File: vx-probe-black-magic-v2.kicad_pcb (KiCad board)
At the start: 2 copper layers, 72.4 x 41.9 mm, 41 parts, among them P1 USB MINI B, P10 CONN_01X01, P11 CONN_01X11, P2 +5v power input, P3 +5v external input, P4 CONN_02X05, P5 CONN_01X04, P6 swdio/jtag, P7 CONN_01X01, P8 CONN_01X01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

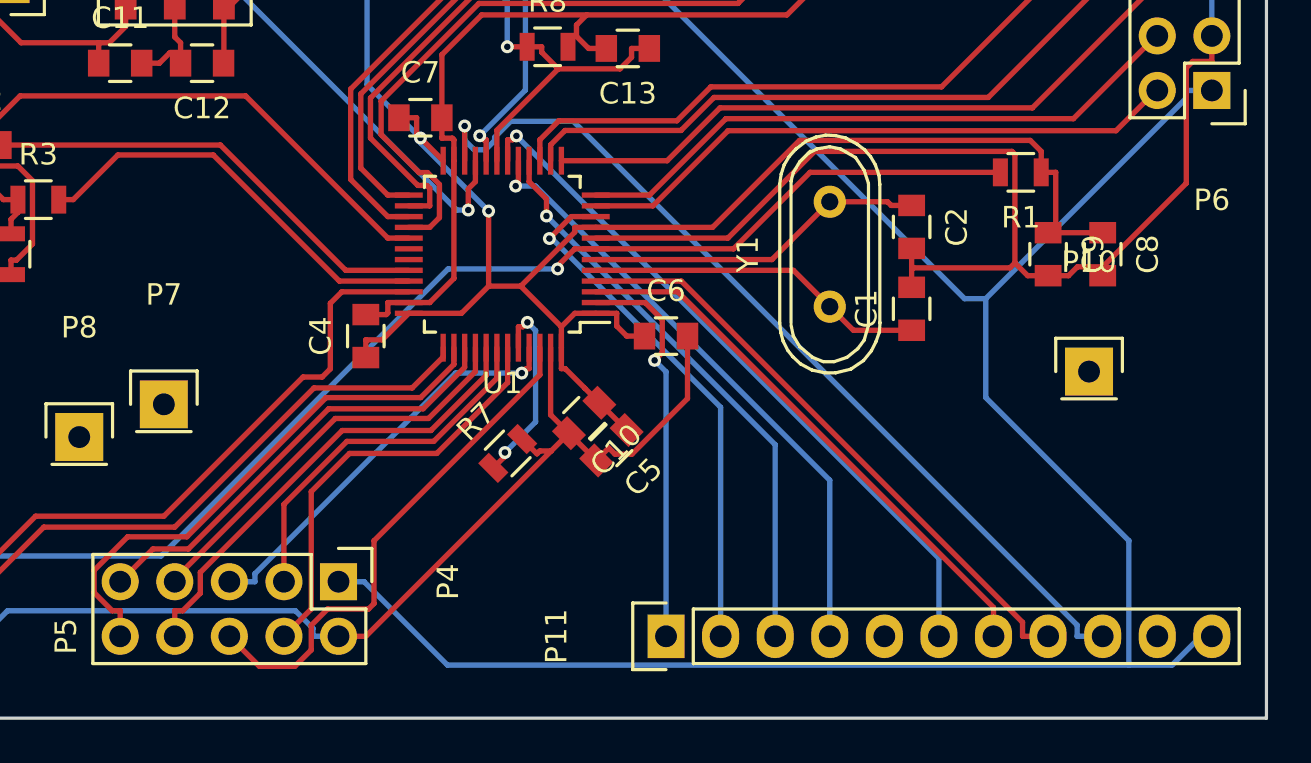
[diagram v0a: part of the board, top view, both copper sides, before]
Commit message: reorganized the unused pins connector
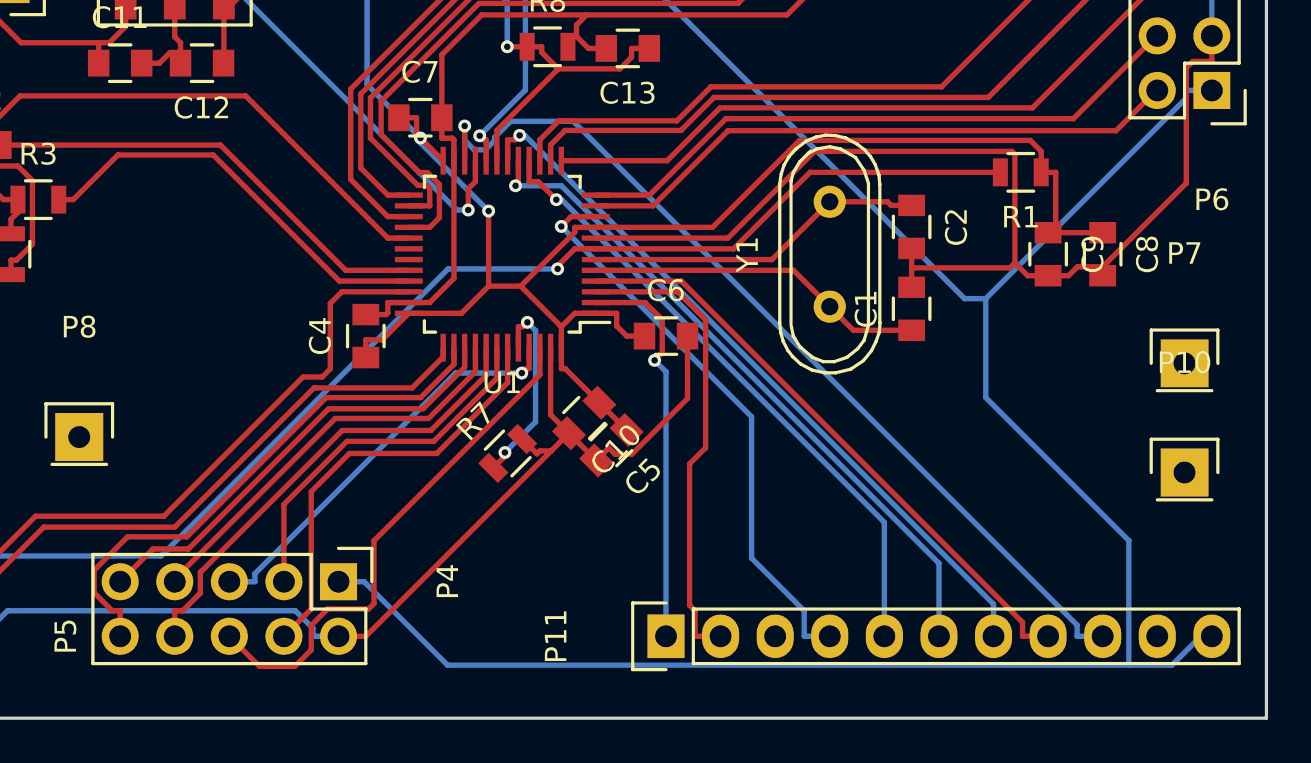
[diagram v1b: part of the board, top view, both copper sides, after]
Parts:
- moved P7 47.5 mm to (115.6, 64.8)
- moved P10 6.47 mm to (115.6, 69.8)
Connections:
- P11 pad 2: /x4 -> /x2
- P11 pad 3: /x5 -> Net-(P11-Pad3)
- P11 pad 4: /x6 -> /x4
- P11 pad 5: Net-(P11-Pad5) -> /x5
- P11 pad 6: /x7 -> /x6
- P11 pad 7: /x2 -> /x7
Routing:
- net /x2: track 25.9 -> 22.0 mm
- net /x6: track 28.8 -> 31.6 mm
- net /x5: track 26.9 -> 29.4 mm
- net /x4: track 24.5 -> 26.7 mm
- net /x7: track 32.9 -> 34.2 mm

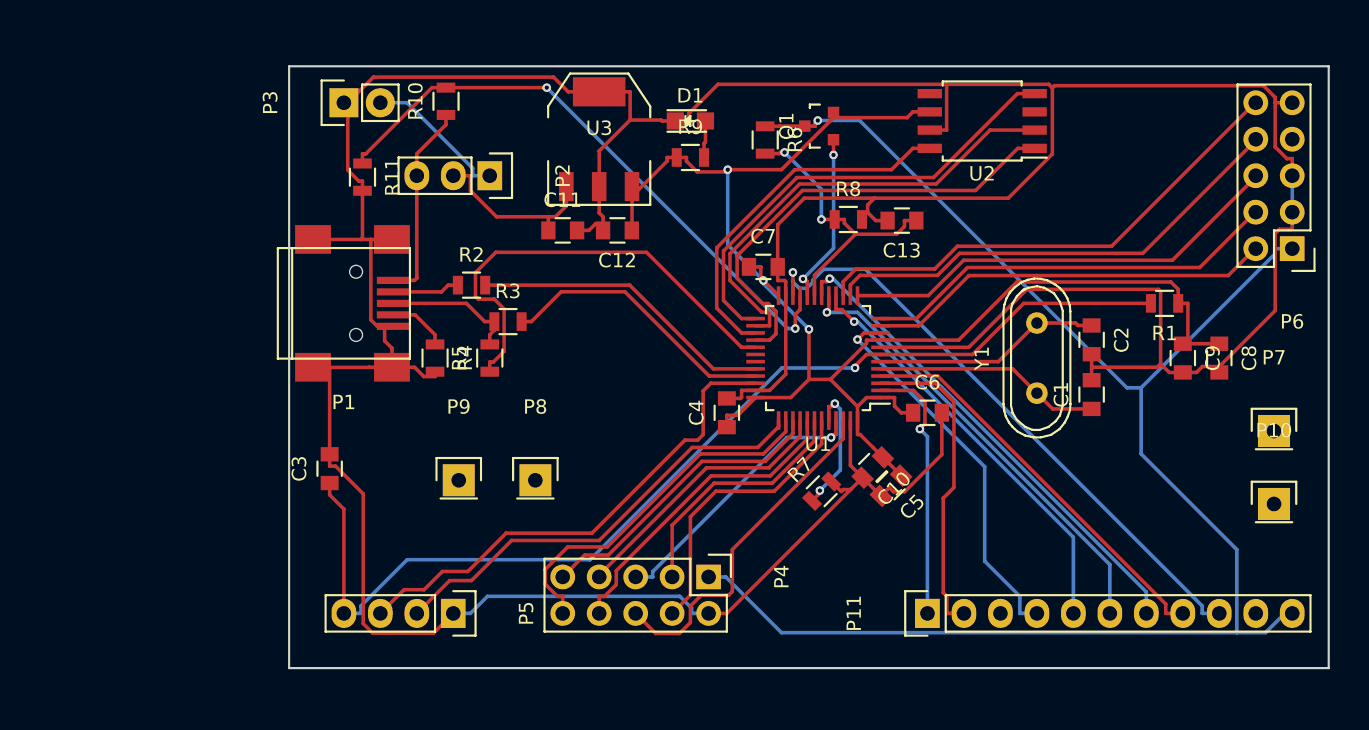
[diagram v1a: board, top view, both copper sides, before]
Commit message: placed and routed the reset button and a serial port
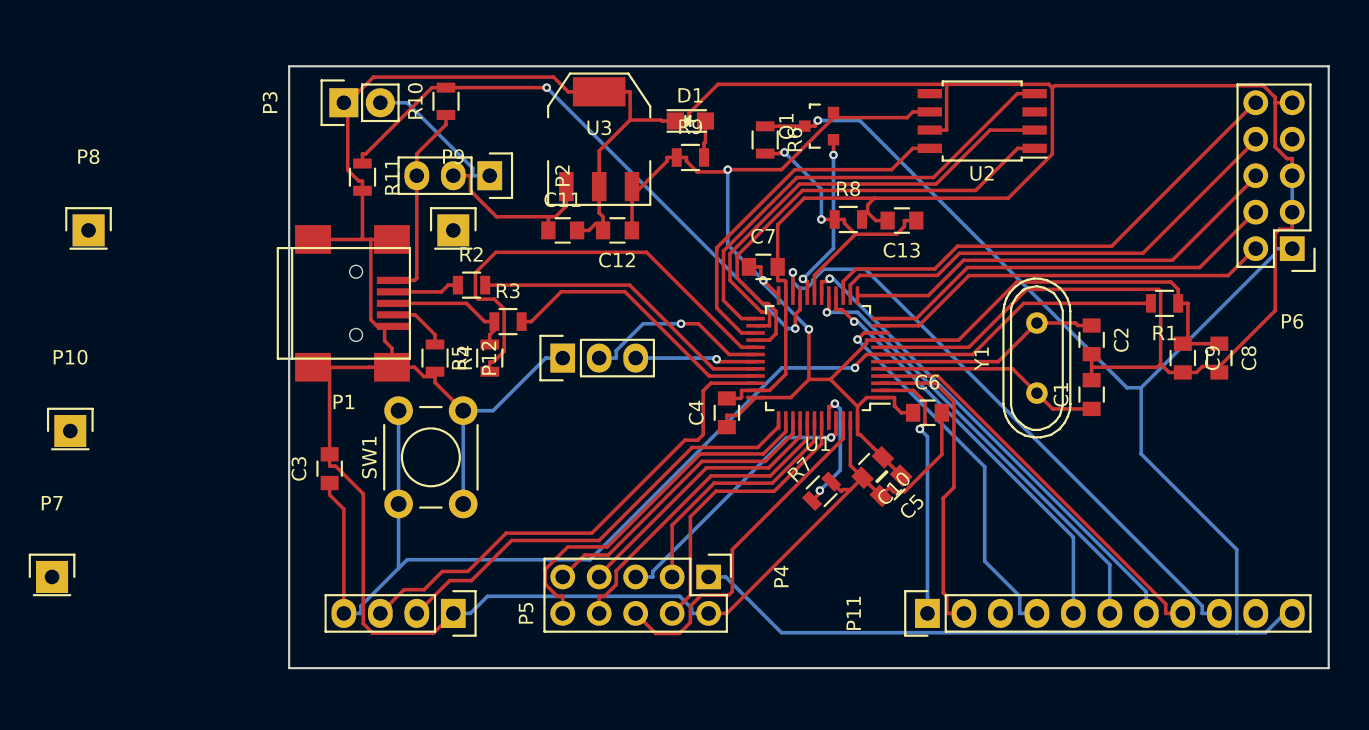
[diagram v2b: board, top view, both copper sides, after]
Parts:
- added P12: CONN_01X03, Pin_Headers:Pin_Header_Straight_1x03, F.Cu at (66.0, 59.7)
- added SW1: SW_PUSH, Buttons_Switches_ThroughHole:SW_PUSH_6mm, F.Cu at (54.6, 69.8)
- moved P7 85.7 mm to (30.5, 74.9)
- moved P10 84.0 mm to (31.8, 64.8)
- moved P8 35.6 mm to (33.0, 50.8)
- moved P9 17.4 mm to (58.4, 50.8)
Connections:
- U1 pad 30: Net-(U1-Pad30) -> /U1_TX
- U1 pad 31: Net-(U1-Pad31) -> /U1_RX
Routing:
- net GND: track 303.7 -> 322.0 mm
- net /U1_TX: track 0.00 -> 13.1 mm, vias 0 -> 1
- net /PROG_NRST: track 75.0 -> 86.0 mm
- net /U1_RX: track 0.00 -> 8.45 mm, vias 0 -> 1

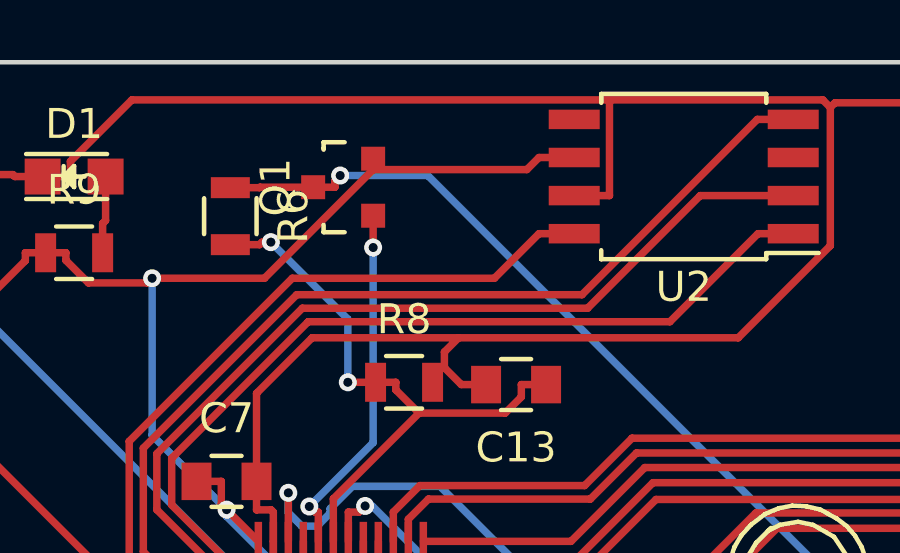
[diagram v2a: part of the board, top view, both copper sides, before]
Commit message: added a pull-up resistor on the target power enable switch (pmosfet)
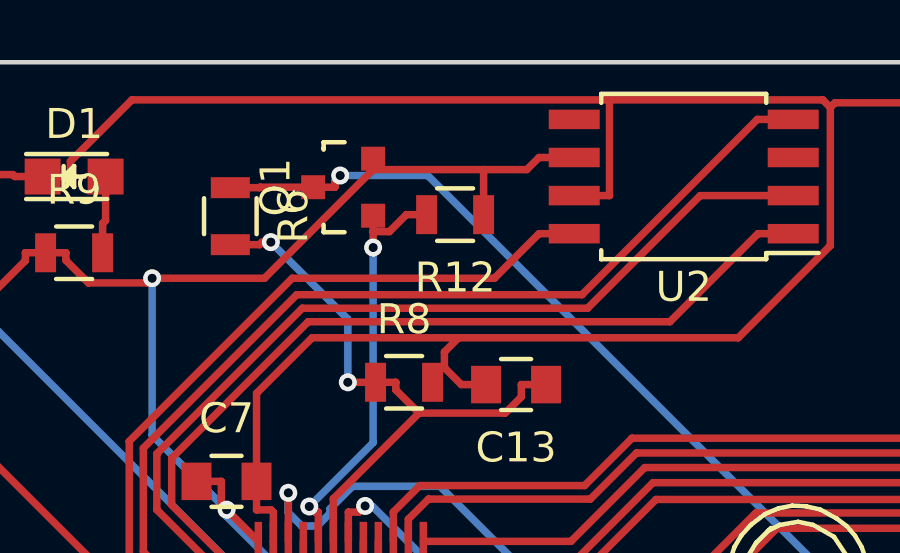
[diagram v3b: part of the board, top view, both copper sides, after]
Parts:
- added R12: 10k, Resistors_SMD:R_0805, F.Cu at (87.6, 44.5)
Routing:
- net /TPWR_CTRL: track 11.9 -> 13.9 mm
- net +3V3: track 105.2 -> 106.7 mm
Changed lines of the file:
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@@
 (kicad_pcb (version 4) (host pcbnew 4.0.4-stable)
   (general
-    (links 117)
-    (no_connects 1)
+    (links 119)
+    (no_connects 0)
     (area 46.914999 39.294999 119.455001 81.355001)
     (thickness 1.6)
     (drawings 11)
-    (tracks 573)
+    (tracks 580)
     (zones 0)
-    (modules 43)
+    (modules 44)
     (nets 59)
   )
@@
       (scale (xyz 1 1 1))
       (rotate (xyz 0 0 90))
+    )
+  )
+  (module Resistors_SMD:R_0805 (layer F.Cu)
+    (at 87.63 44.45 180)
+    (descr "Resistor SMD 0805, reflow soldering, Vishay (see dcrcw.pdf)")
+    (tags "resistor 0805")
+    (attr smd)
+    (fp_text reference R12 (at 0 -2.1 180) (layer F.SilkS)
+      (effects (font (size 1 1) (thickness 0.15)))
+    )
+    (fp_text value 10k (at 0 2.1 180) (layer F.Fab)
+      (effects (font (size 1 1) (thickness 0.15)))
+    )
+    (fp_line (start -1.6 -1) (end 1.6 -1) (layer F.CrtYd) (width 0.05))
+    (fp_line (start -1.6 1) (end 1.6 1) (layer F.CrtYd) (width 0.05))
+    (fp_line (start -1.6 -1) (end -1.6 1) (layer F.CrtYd) (width 0.05))
+    (fp_line (start 1.6 -1) (end 1.6 1) (layer F.CrtYd) (width 0.05))
+    (fp_line (start 0.6 0.875) (end -0.6 0.875) (layer F.SilkS) (width 0.15))
+    (fp_line (start -0.6 -0.875) (end 0.6 -0.875) (layer F.SilkS) (width 0.15))
+    (pad 1 smd rect (at -0.95 0 180) (size 0.7 1.3) (layers F.Cu F.Paste F.Mask)
+      (net 4 +3V3))
+    (pad 2 smd rect (at 0.95 0 180) (size 0.7 1.3) (layers F.Cu F.Paste F.Mask)
+      (net 38 /TPWR_CTRL))
+    (model Resistors_SMD.3dshapes/R_0805.wrl
+      (at (xyz 0 0 0))
+      (scale (xyz 1 1 1))
+      (rotate (xyz 0 0 0))
     )
   )
@@
   (segment (start 108.9 55.88) (end 108.9 54.9047) (width 0.25) (layer F.Cu) (net 4))
   (segment (start 84.897 42.5856) (end 84.897 42.9482) (width 0.25) (layer F.Cu) (net 4))
-  (segment (start 90.0215 42.9482) (end 84.897 42.9482) (width 0.25) (layer F.Cu) (net 4))
+  (segment (start 81.2754 46.5698) (end 84.897 42.9482) (width 0.25) (layer F.Cu) (net 4))
+  (segment (start 77.5298 46.5698) (end 81.2754 46.5698) (width 0.25) (layer F.Cu) (net 4))
+  (segment (start 90.0215 42.9482) (end 88.5758 42.9482) (width 0.25) (layer F.Cu) (net 4))
   (segment (start 90.4247 42.545) (end 90.0215 42.9482) (width 0.25) (layer F.Cu) (net 4))
   (segment (start 91.6 42.545) (end 90.4247 42.545) (width 0.25) (layer F.Cu) (net 4))
-  (segment (start 81.2754 46.5698) (end 84.897 42.9482) (width 0.25) (layer F.Cu) (net 4))
-  (segment (start 77.5298 46.5698) (end 81.2754 46.5698) (width 0.25) (layer F.Cu) (net 4))
+  (segment (start 88.5758 42.9482) (end 84.897 42.9482) (width 0.25) (layer F.Cu) (net 4))
+  (segment (start 88.58 42.9524) (end 88.58 44.45) (width 0.25) (layer F.Cu) (net 4))
+  (segment (start 88.5758 42.9482) (end 88.58 42.9524) (width 0.25) (layer F.Cu) (net 4))
   (segment (start 109.22 58.69) (end 109.575 58.69) (width 0.25) (layer F.Cu) (net 4))
   (segment (start 109.575 58.69) (end 111.76 58.69) (width 0.25) (layer F.Cu) (net 4))
@@
   (segment (start 84.897 52.0507) (end 84.897 45.5458) (width 0.25) (layer B.Cu) (net 38))
   (segment (start 82.7694 54.1783) (end 84.897 52.0507) (width 0.25) (layer B.Cu) (net 38))
-  (segment (start 84.897 45.5458) (end 84.897 44.4856) (width 0.25) (layer F.Cu) (net 38))
+  (segment (start 85.439 45.0157) (end 84.897 45.0157) (width 0.25) (layer F.Cu) (net 38))
+  (segment (start 86.0047 44.45) (end 85.439 45.0157) (width 0.25) (layer F.Cu) (net 38))
+  (segment (start 86.68 44.45) (end 86.0047 44.45) (width 0.25) (layer F.Cu) (net 38))
+  (segment (start 84.897 45.5458) (end 84.897 45.0157) (width 0.25) (layer F.Cu) (net 38))
+  (segment (start 84.897 45.0157) (end 84.897 44.4856) (width 0.25) (layer F.Cu) (net 38))
   (segment (start 78.4947 58.94) (end 79.47 58.94) (width 0.25) (layer F.Cu) (net 39))
   (segment (start 71.8787 52.324) (end 78.4947 58.94) (width 0.25) (layer F.Cu) (net 39))

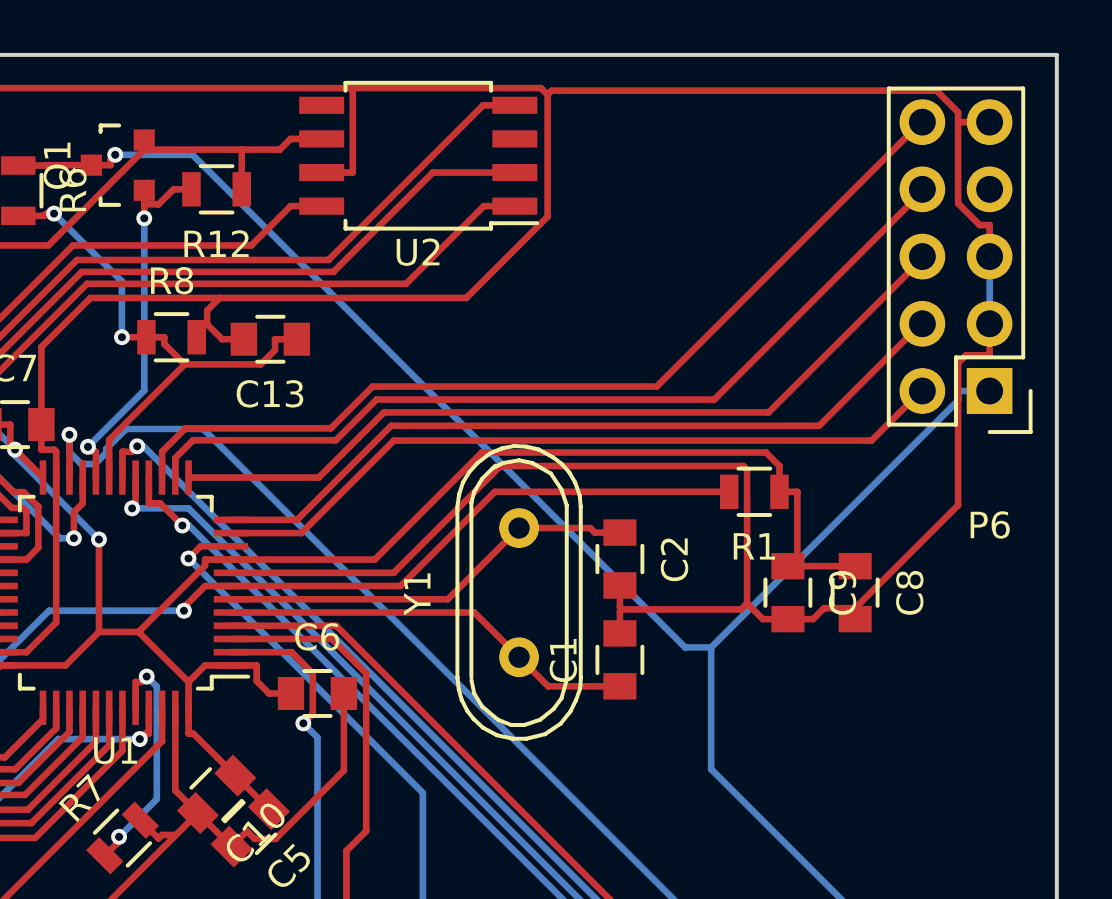
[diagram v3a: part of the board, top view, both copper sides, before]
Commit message: moved the crystal closer to the microcontroller
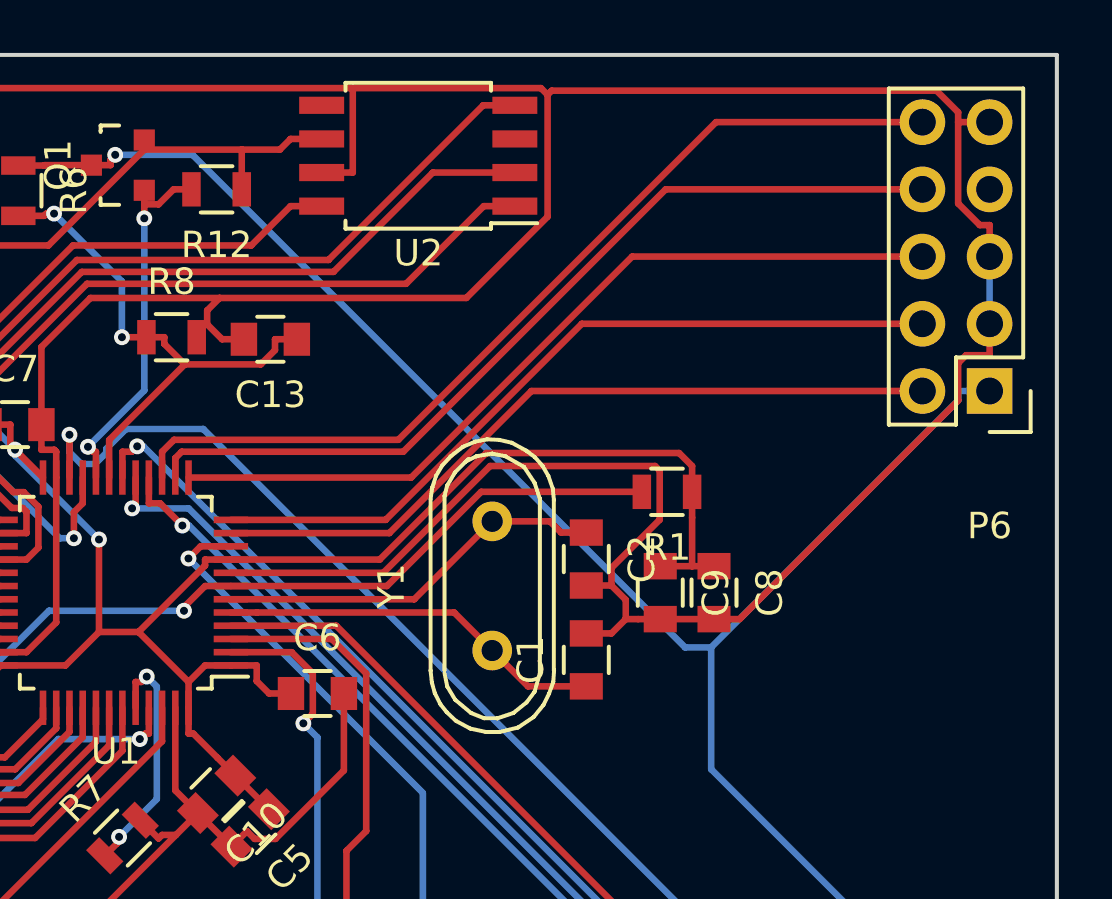
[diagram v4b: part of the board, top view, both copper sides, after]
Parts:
- moved C8 5.33 mm to (106.4, 59.7)
- moved C9 4.83 mm to (104.4, 59.7)
- moved R1 3.30 mm to (104.6, 55.9)
- moved C1 1.27 mm to (101.6, 62.2)
- moved C2 1.27 mm to (101.6, 58.4)
- moved Y1 1.05 mm to (98.0, 59.4)
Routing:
- net +3V3: track 106.7 -> 102.2 mm
- net GND: track 322.0 -> 317.9 mm
- net /PROG_NRST: track 86.0 -> 82.7 mm
- net Net-(C1-Pad1): track 15.9 -> 14.6 mm
- net Net-(C2-Pad1): track 15.9 -> 14.8 mm
